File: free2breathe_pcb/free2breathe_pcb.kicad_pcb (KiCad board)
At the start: 2 copper layers, 108.5 x 115 mm, 101 parts, among them J1 USB4110-GF-A_REVB, J2 LED_Connector, J3 Alarm_Connector, Q1 AO3401A, Q2 DMN3404L, U1 IP5328, U2 MCP6044-E/P, U3 MCP6044-E/P, U4 SO2 Sensor, U5 CO Sensor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

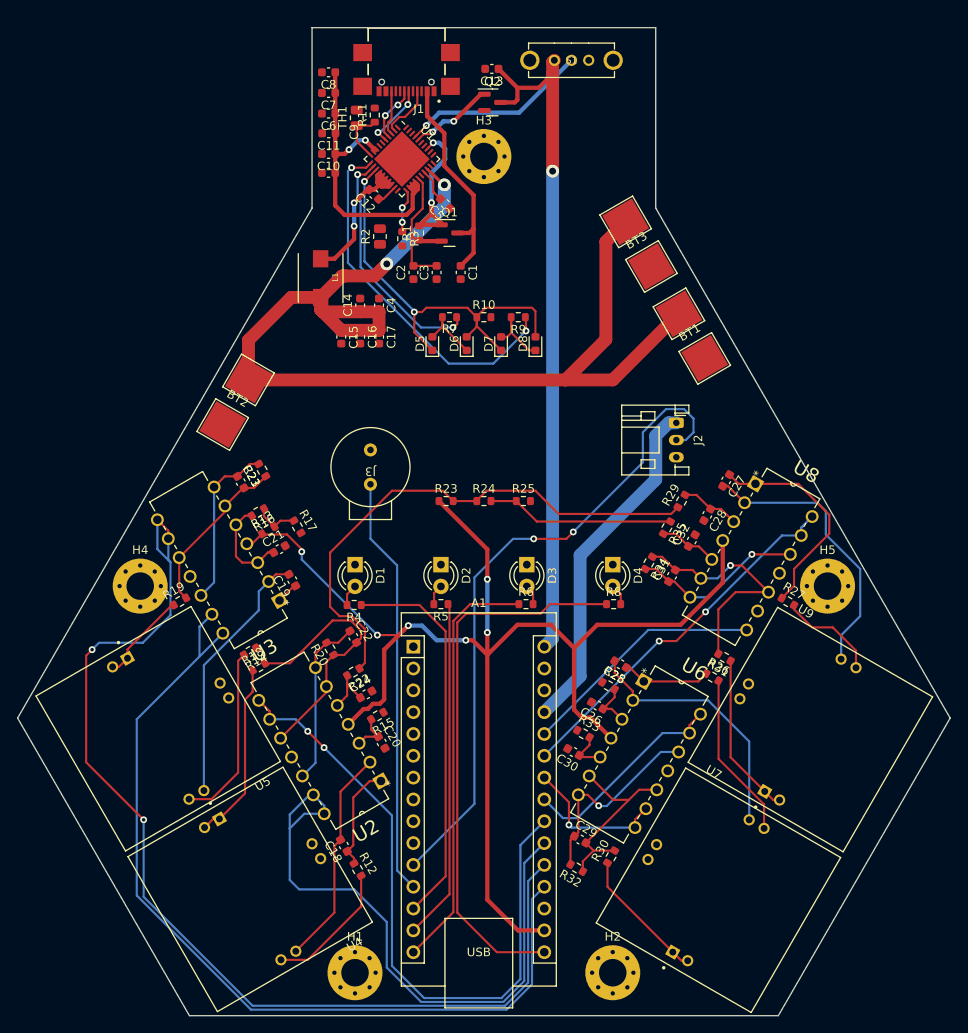
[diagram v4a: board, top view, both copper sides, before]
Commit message: further routing, ground planes and sticthing vias
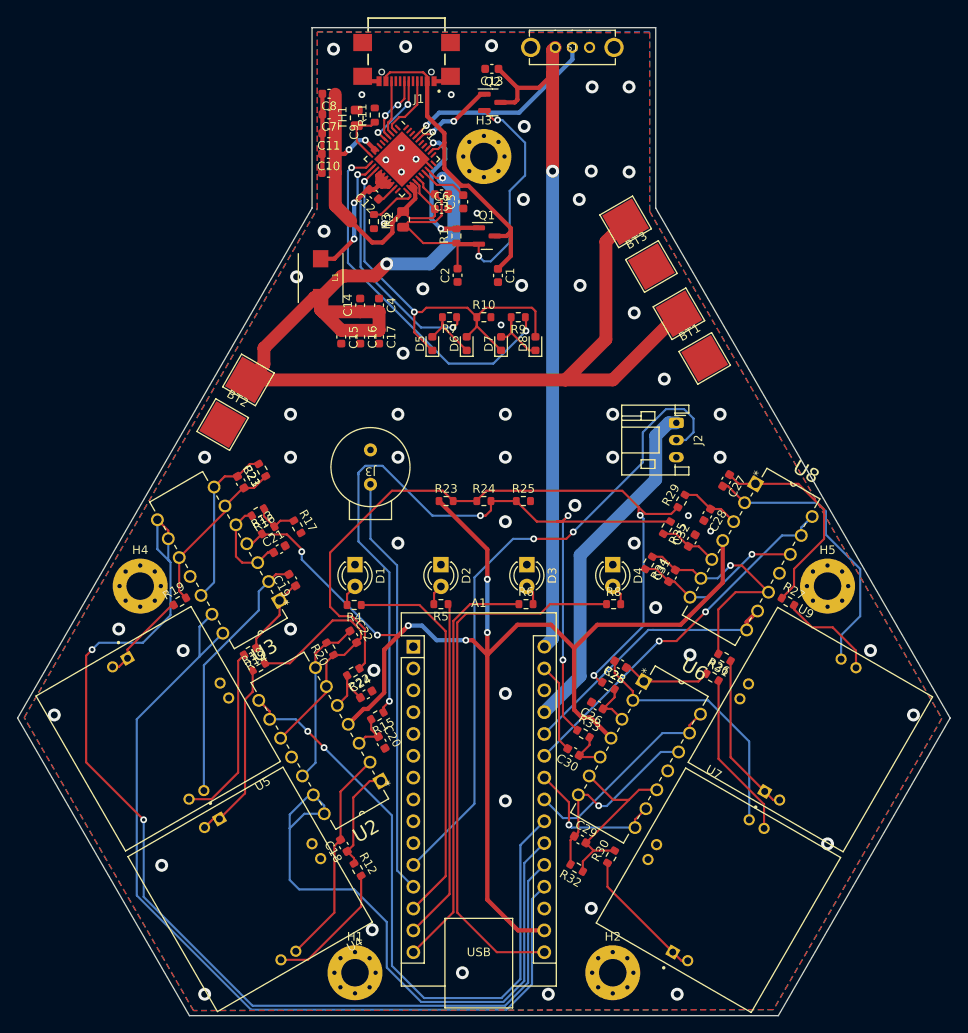
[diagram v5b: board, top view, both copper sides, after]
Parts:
- moved C6 17.2 mm to (115.1, 71.1), turned to 0 degrees
- moved C3 9.12 mm to (115.1, 69.4), turned to 180 degrees
- moved C2 5.15 mm to (116.9, 78.8)
- moved C1 4.35 mm to (121.6, 78.8)
- moved Q1 4.35 mm to (120.3, 74.2)
- moved R1 4.35 mm to (116.8, 74.2)
- moved R3 3.86 mm to (107.2, 72.6)
- moved R2 3.36 mm to (110.6, 72.3)
- moved C7 2.50 mm to (102.0, 60.1)
- moved C8 2.50 mm to (102.0, 57.7)
- moved C5 2.11 mm to (117.6, 70.3), turned to 90 degrees
- moved S1 1.50 mm to (130.3, 52.3)
- moved J1 1.17 mm to (111.0, 55.2)
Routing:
- net /Divider_Low: track 21.9 -> 98.5 mm, vias 0 -> 4
- net /VMID: track 17.4 -> 48.1 mm, vias 0 -> 2
- net GND: track 0.00 -> 27.6 mm, vias 0 -> 63
- net /Divider_High: track 62.2 -> 85.8 mm, vias 0 -> 2
- net /VBAT+: track 134.5 -> 147.2 mm
- net /VBUS: track 25.2 -> 37.4 mm
- net /VSYS: track 36.4 -> 44.6 mm
- net Net-(C19-Pad1): track 2.57 -> 9.21 mm
- net /Arduino_A7: track 28.6 -> 31.3 mm
- net /VREG: track 3.91 -> 5.63 mm
- net /VOUT: track 80.1 -> 81.6 mm
- net Net-(S1-Pad2): track 21.9 -> 23.4 mm
- net /VBUSG: track 18.6 -> 17.4 mm
- net /DPC: track 7.65 -> 8.82 mm
- net /DMC: track 6.70 -> 7.87 mm
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- added copper zone on B.Cu, net GND
- added copper zone on F.Cu, net GND

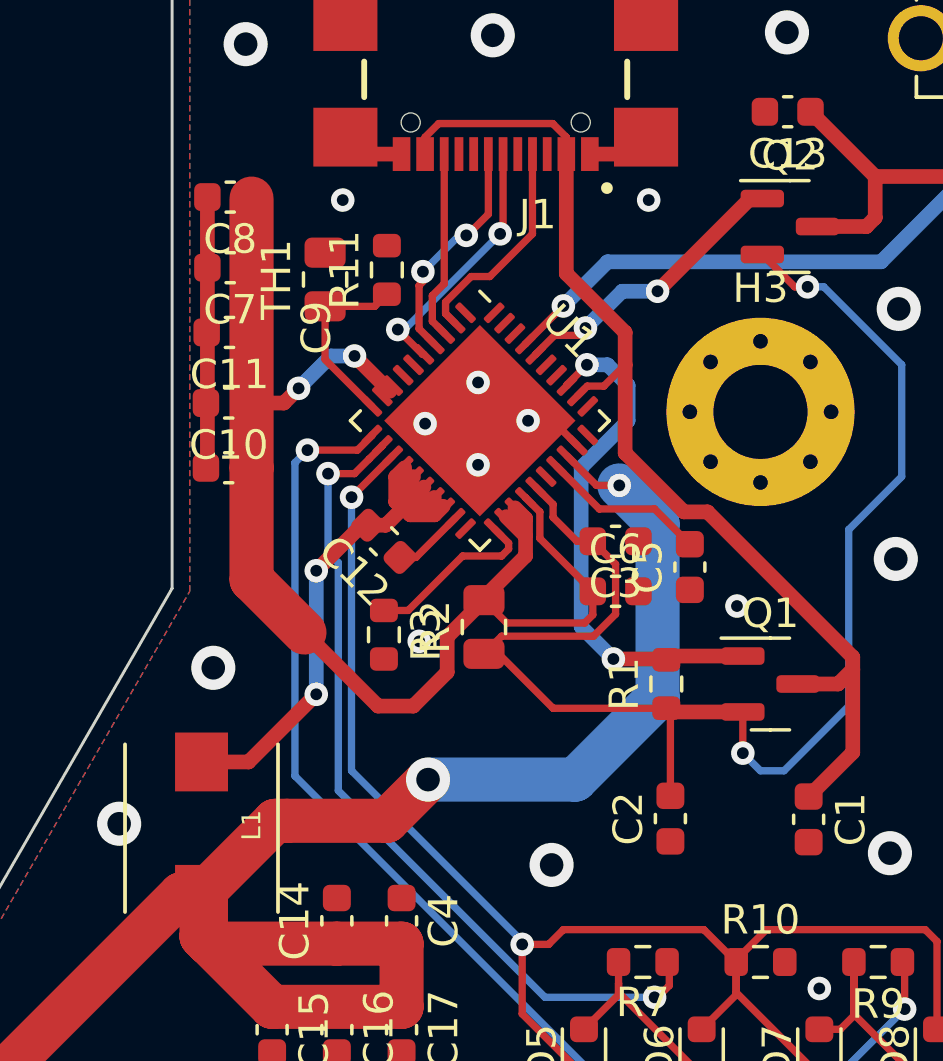
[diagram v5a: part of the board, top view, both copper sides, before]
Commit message: add BOM, update board with component replacements
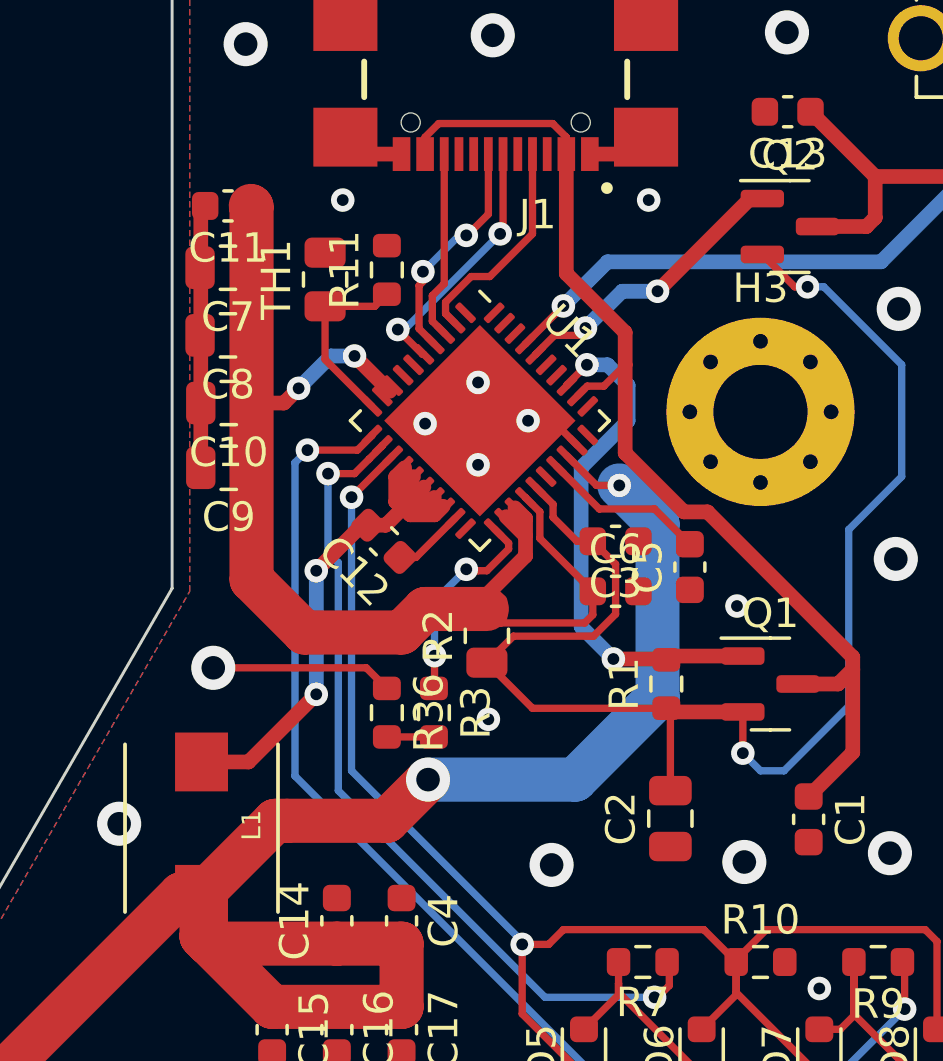
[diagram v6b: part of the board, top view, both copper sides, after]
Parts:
- added R36: 14k 0.1%, Resistor_SMD:R_0603_1608Metric, F.Cu at (107.3, 75.2)
- C10, C2, C7, C8, C9: footprint Capacitor_SMD:C_0603_1608Metric -> Capacitor_SMD:C_0805_2012Metric
- R3: value 114k 1% -> 100k 0.1%
- moved C8 4.70 mm to (101.9, 62.4)
- moved C11 4.30 mm to (101.9, 58.0)
- moved R3 3.15 mm to (108.9, 75.2)
- moved R2 0.32 mm to (110.7, 72.6)
- moved C7 0.07 mm to (101.9, 60.1)
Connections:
- R3 pad 2: GND -> Net-(R3-Pad2)
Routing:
- net GND: track 27.6 -> 33.8 mm, vias 63 -> 64
- net /VSYS: track 44.6 -> 41.5 mm
- net Net-(R3-Pad2): track 0.00 -> 1.60 mm
- net Net-(R3-Pad1): track 6.00 -> 7.17 mm, vias 0 -> 2
